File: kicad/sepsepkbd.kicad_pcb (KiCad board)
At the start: 2 copper layers, 202.9 x 111.3 mm, 47 parts, among them J1 MJ-4PP-9, J2 Conn_01x04_Socket, J3 Conn_01x04_Socket, SW1 SW_PUSH, SW10 SW_PUSH, SW11 SW_PUSH, SW12 SW_PUSH, SW13 SW_PUSH, SW14 SW_PUSH, SW15 SW_PUSH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

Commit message: 2.1
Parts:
- removed SW_RESET1: SW_PUSH, kbd:ResetSW
- added D22: D, kbd:D3_SMD_v2, B.Cu at (118.4, 118.9)
- added J4: Conn_01x10_Pin, Connector_PinHeader_2.54mm:PinHeader_1x10_P2.54mm_Vertical, F.Cu at (97.0, 93.9)
- added J5: Conn_01x10_Pin, Connector_PinHeader_2.54mm:PinHeader_1x10_P2.54mm_Vertical, F.Cu at (144.6, 93.9)
- added J6: Conn_01x08_Pin, Connector_PinHeader_2.54mm:PinHeader_1x08_P2.54mm_Vertical, F.Cu at (180.3, 97.7)
- added J7: Conn_01x08_Pin, Connector_PinHeader_2.54mm:PinHeader_1x08_P2.54mm_Vertical, F.Cu at (82.9, 97.7)
- added SW22: SW_PUSH, keyswitches:Kailh_socket_PG1350, F.Cu at (148.6, 128.6)
- added U2: RP2040-Zero, isw-kbd:RP2040-Zero-THT, F.Cu at (97.7, 107.7)
- D20, D21: footprint kbd:D3_SMD -> kbd:D3_SMD_v2; moved to B.Cu
- J1: footprint kbd:MJ-4PP-9 -> kbd:MJ-4PP-9_1side
- J2: value Conn_01x04_Socket -> MJ-4PP-9; footprint Connector_PinHeader_2.54mm:PinHeader_1x04_P2.54mm_Horizontal -> kbd:MJ-4PP-9_1side
- J3: value Conn_01x04_Socket -> Conn_01x10_Pin; footprint Connector_PinHeader_2.54mm:PinHeader_1x04_P2.54mm_Horizontal -> Connector_PinHeader_2.54mm:PinHeader_1x10_P2.54mm_Vertical
- SW1, SW10, SW11, SW12, SW13, SW14, SW15, SW16, SW17, SW18, SW2, SW3, SW4, SW5, SW6, SW7, SW8, SW9: footprint keyswitches:SW_PG1350_reversible -> keyswitches:Kailh_socket_PG1350_reversible
- SW19: footprint keyswitches:SW_PG1350_reversible -> kbd:ResetSW
- SW20, SW21: footprint keyswitches:SW_PG1350_reversible -> keyswitches:Kailh_socket_PG1350
- U1: value ProMicro -> RP2040-Zero; footprint kbd:ProMicro_v2 -> isw-kbd:RP2040-Zero-THT
- moved J2 87.9 mm to (77.1, 123.5), turned to 90 degrees
- moved SW19 87.2 mm to (148.1, 55.8), turned to -90 degrees
- moved J1 84.2 mm to (185.9, 123.4), turned to -90 degrees
- moved SW20 79.3 mm to (115.0, 128.6), turned to 45 degrees
- moved J3 69.3 mm to (97.0, 78.0), turned to 90 degrees
- moved SW21 54.8 mm to (131.8, 118.5), turned to 45 degrees
- moved D19 53.1 mm to (143.4, 56.0), turned to 90 degrees
- moved U1 51.8 mm to (165.9, 107.7)
- moved D21 35.7 mm to (135.0, 108.7), turned to -45 degrees
- moved D17 31.1 mm to (114.4, 60.5), turned to -90 degrees
- moved D16 31.1 mm to (95.4, 60.5), turned to -90 degrees
- moved D15 31.1 mm to (76.4, 60.5), turned to -90 degrees
- moved D14 31.1 mm to (57.4, 60.5), turned to -90 degrees
- moved D13 31.1 mm to (38.4, 60.5), turned to -90 degrees
- moved D6 31.1 mm to (133.4, 22.5), turned to -90 degrees
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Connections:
- D1 pad 1: row0 -> /t_row0
- D10 pad 1: row1 -> /t_row1
- D11 pad 1: row1 -> /t_row1
- D12 pad 1: row1 -> /t_row1
- D13 pad 1: row2 -> /t_row2
- D14 pad 1: row2 -> /t_row2
- D15 pad 1: row2 -> /t_row2
- D16 pad 1: row2 -> /t_row2
- D17 pad 1: row2 -> /t_row2
- D18 pad 1: row2 -> /t_row2
- D19 pad 1: Net-(D19-K) -> /t_row2
- D2 pad 1: row0 -> /t_row0
- D20 pad 1: Net-(D19-K) -> bu1_row3
- D21 pad 1: Net-(D19-K) -> bu1_row3
- D3 pad 1: row0 -> /t_row0
- D4 pad 1: row0 -> /t_row0
- D5 pad 1: row0 -> /t_row0
- D6 pad 1: row0 -> /t_row0
- D7 pad 1: row1 -> /t_row1
- D8 pad 1: row1 -> /t_row1
- D9 pad 1: row1 -> /t_row1
- J1 pad D: VCC -> u1_3.3v
- J3 pad 1: Net-(D19-K) -> /t_row0
- J3 pad 2: Net-(J3-Pin_2) -> /t_row1
- J3 pad 3: Net-(J3-Pin_3) -> /t_row2
- J3 pad 4: Net-(J3-Pin_4) -> /t_col0
- SW1 pad 1: col0 -> /t_col0
- SW10 pad 1: col3 -> /t_col3
- SW11 pad 1: col4 -> /t_col4
- SW12 pad 1: col5 -> /t_col5
- SW13 pad 1: col0 -> /t_col0
- SW14 pad 1: col1 -> /t_col1
- SW15 pad 1: col2 -> /t_col2
- SW16 pad 1: col3 -> /t_col3
- SW17 pad 1: col4 -> /t_col4
- SW18 pad 1: col5 -> /t_col5
- SW19 pad 1: Net-(J3-Pin_2) -> /t_col6
- SW2 pad 1: col1 -> /t_col1
- SW20 pad 1: Net-(J3-Pin_3) -> bu1_col4
- SW21 pad 1: Net-(J3-Pin_4) -> bu1_col5
- SW3 pad 1: col2 -> /t_col2
- SW4 pad 1: col3 -> /t_col3
- SW5 pad 1: col4 -> /t_col4
- SW6 pad 1: col5 -> /t_col5
- SW7 pad 1: col0 -> /t_col0
- SW8 pad 1: col1 -> /t_col1
- SW9 pad 1: col2 -> /t_col2
- U1 pad 1: unconnected-(U1-TX0/D3-Pad1)_0 -> bu1_col0
- U1 pad 10: row3 -> bu1_op2
- U1 pad 11: unconnected-(U1-8/B4-Pad11)_0 -> bu1_op3
- U1 pad 12: unconnected-(U1-9/B5-Pad12) -> bu1_op4
- U1 pad 13: unconnected-(U1-B6/10-Pad13) -> bu1_op5
- U1 pad 15: col5 -> unconnected-(U1-Pad15)
- U1 pad 2: data -> bu1_col1
- U1 pad 3: GND -> bu1_col2
- U1 pad 4: GND -> bu1_col3
- U1 pad 5: unconnected-(U1-2/D1/SDA-Pad5) -> bu1_col4
- U1 pad 6: unconnected-(U1-3/D0/SCL-Pad6) -> bu1_col5
- U1 pad 7: row0 -> bu1_col6
- U1 pad 8: row1 -> unconnected-(U1-Pad8)
- U1 pad 9: row2 -> bu1_op1
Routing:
- net /t_row0: track 0.00 -> 263.0 mm, vias 0 -> 1
- net row0: track 259.1 -> 0.00 mm, vias 1 -> 0
- net row2: track 242.0 -> 0.00 mm, vias 1 -> 0
- net col0: track 176.2 -> 0.00 mm, vias 1 -> 0
- net col3: track 168.2 -> 0.00 mm, vias 2 -> 0
- net col1: track 154.0 -> 0.00 mm, vias 1 -> 0
- net /t_col0: track 0.00 -> 144.3 mm, vias 0 -> 3
- net /t_row1: track 0.00 -> 143.5 mm, vias 0 -> 6
- net GND: track 51.9 -> 195.1 mm
- net bu1_col5: track 0.00 -> 140.0 mm, vias 0 -> 3
- net row1: track 139.5 -> 0.00 mm, vias 6 -> 0
- net bu1_col6: track 0.00 -> 138.3 mm, vias 0 -> 2
- net col2: track 133.4 -> 0.00 mm, vias 1 -> 0
- net /t_col1: track 0.00 -> 131.7 mm, vias 0 -> 3
- net bu1_col4: track 0.00 -> 130.5 mm, vias 0 -> 2
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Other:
- board size 202.9 x 111.3 mm -> 170.7 x 127.7 mm
- board text removed: "sep/sep"

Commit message: update
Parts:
- moved D19 2.44 mm to (141.0, 56.2)
- moved SW19 2.44 mm to (145.7, 56.0)
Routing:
- net /t_row2: track 130.4 -> 127.9 mm
- net /t_col6: track 36.1 -> 34.9 mm
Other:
- outline, holes or cut-outs redrawn

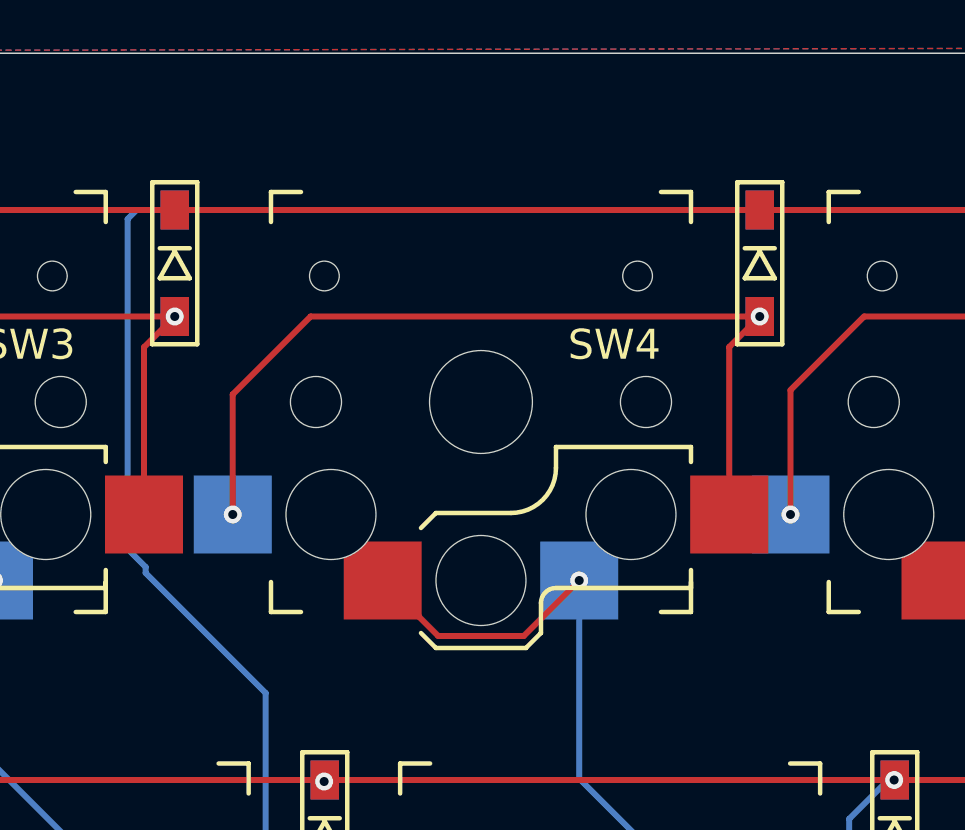
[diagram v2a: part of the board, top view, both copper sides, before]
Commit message: スイッチのズレ修正
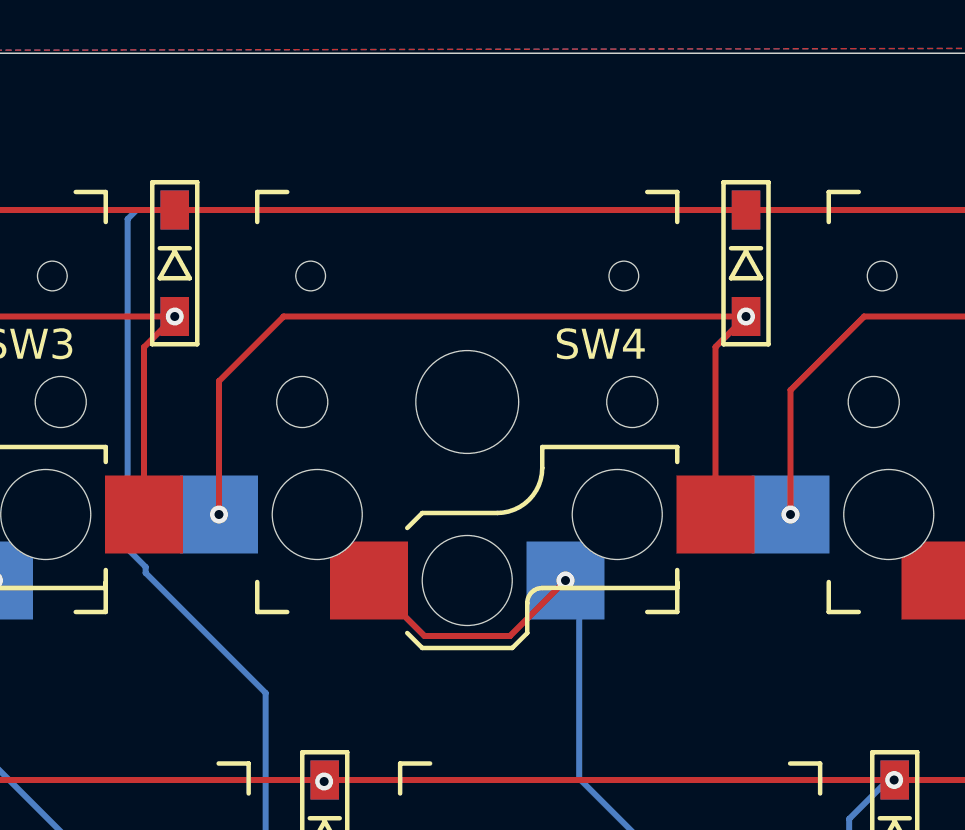
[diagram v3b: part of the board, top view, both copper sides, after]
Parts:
- moved D4 0.46 mm to (95.5, 22.5)
- moved SW4 0.46 mm to (86.2, 27.1)
